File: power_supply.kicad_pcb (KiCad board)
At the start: 2 copper layers, 27 parts, among them T1 Transformer_SP_1S, U1 LM317_TO-220, U2 LM337_TO220, U3 LM385BZ-1.2, U4 LM385BZ-1.2

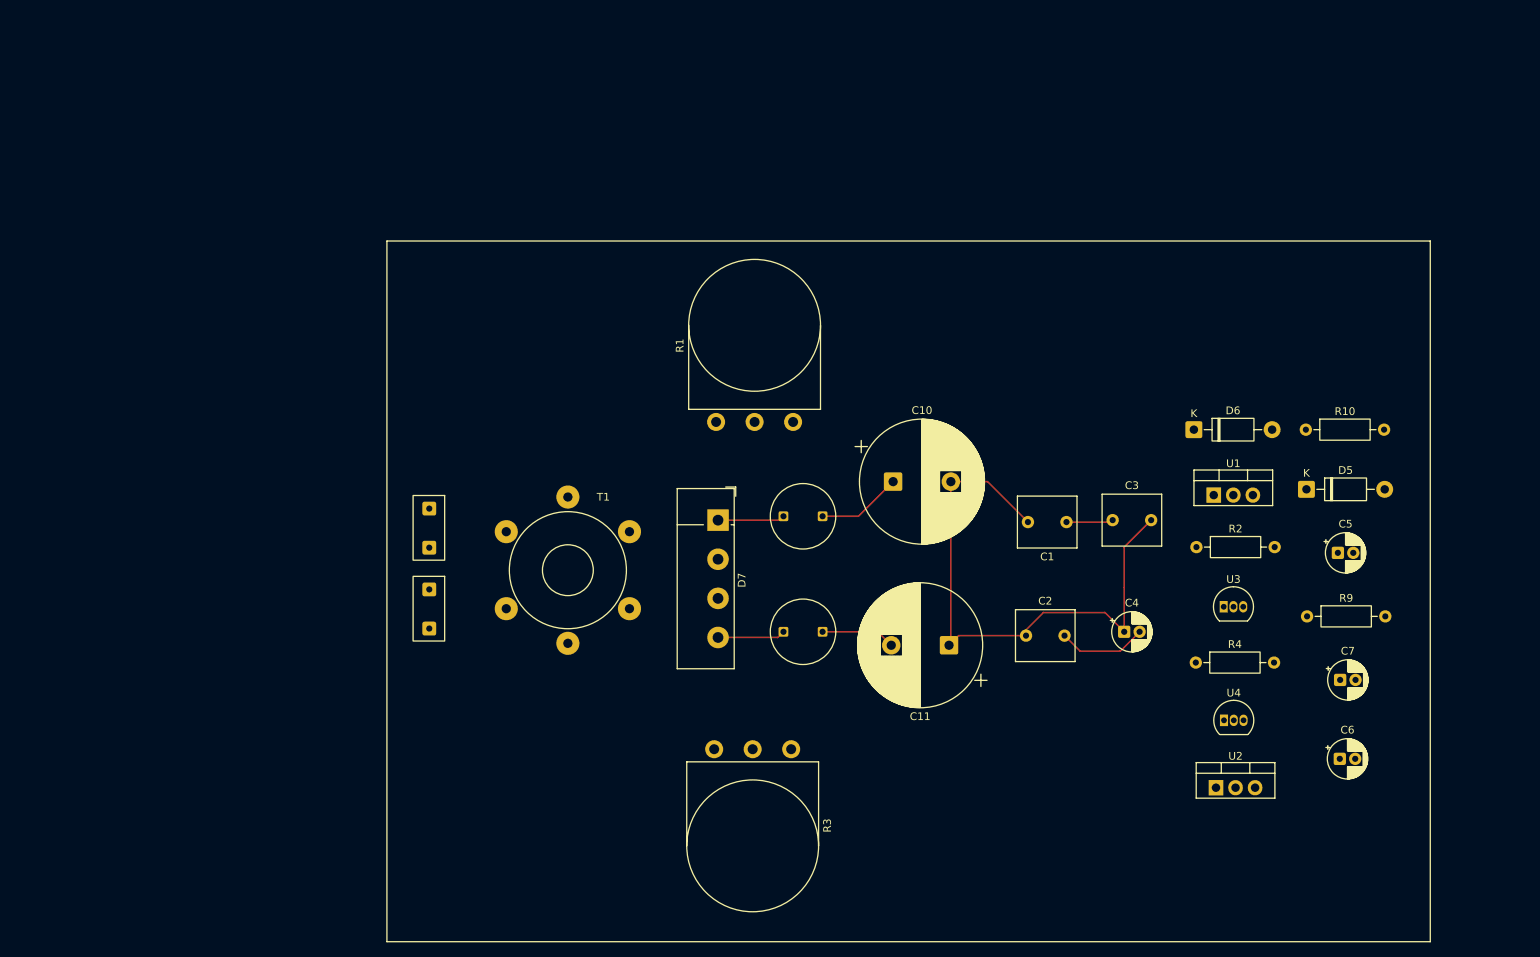
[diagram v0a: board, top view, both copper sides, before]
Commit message: inital version of traces and GND zonefill
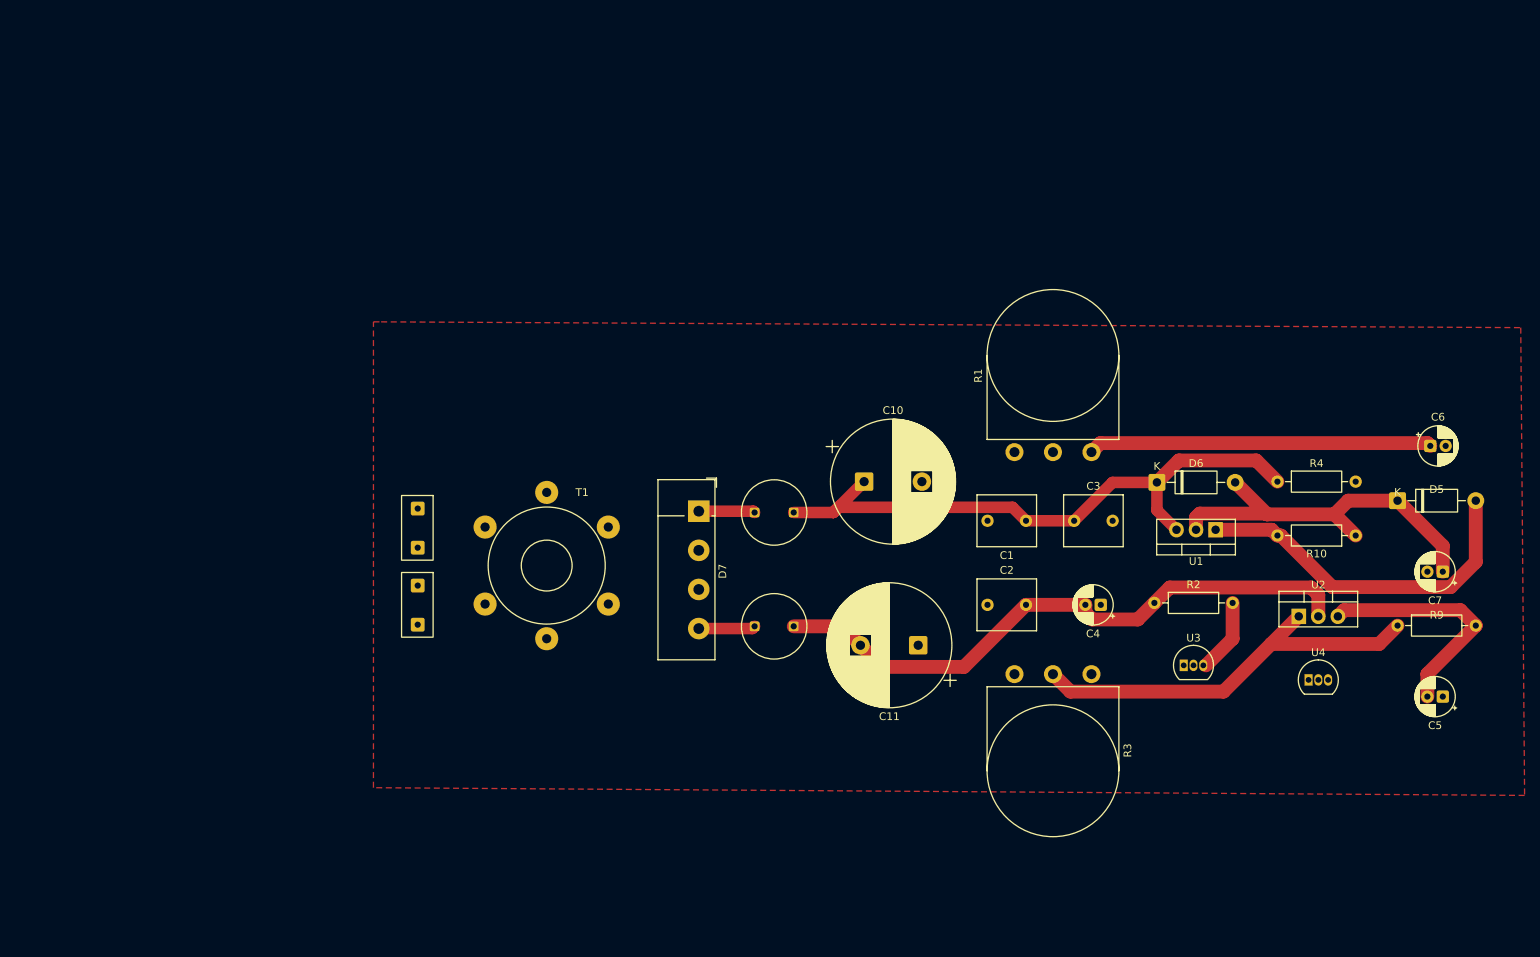
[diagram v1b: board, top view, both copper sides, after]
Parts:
- moved C6 42.3 mm to (211.8, 82.1)
- moved R3 40.2 mm to (157.8, 111.8)
- moved R1 38.9 mm to (167.8, 82.9)
- moved R4 25.8 mm to (191.9, 86.8)
- moved U2 24.7 mm to (194.7, 104.2)
- moved C5 23.1 mm to (213.4, 114.7), turned to 180 degrees
- moved C7 19.4 mm to (213.4, 98.4), turned to 180 degrees
- moved R10 15.2 mm to (202.1, 93.8), turned to 180 degrees
- moved U4 12.2 mm to (195.9, 112.5)
- moved D5 11.9 mm to (207.5, 89.2)
- moved R9 11.8 mm to (207.5, 105.4)
- moved U3 9.21 mm to (179.7, 110.6)
- moved R2 9.08 mm to (175.9, 102.5)
- moved D6 8.36 mm to (176.2, 86.8)
- moved C2 6.40 mm to (154.2, 102.8)
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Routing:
- net Net-(D5-A): track 0.00 -> 90.8 mm
- net GND: track 75.5 -> 0.35 mm
- net Net-(D6-K): track 17.1 -> 82.2 mm
- net Net-(U2-VI): track 21.3 -> 79.9 mm
- net Net-(U2-ADJ): track 0.00 -> 54.3 mm
- net /0-15V: track 0.00 -> 50.2 mm
- net /0-(-15)V: track 0.00 -> 30.9 mm
- net Net-(U3-A): track 0.00 -> 9.63 mm
- net Net-(D7--): track 8.81 -> 7.37 mm
- net Net-(D7-+): track 8.71 -> 7.32 mm
- added copper zone on F.Cu, net GND

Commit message: added connectors, traces and second layer
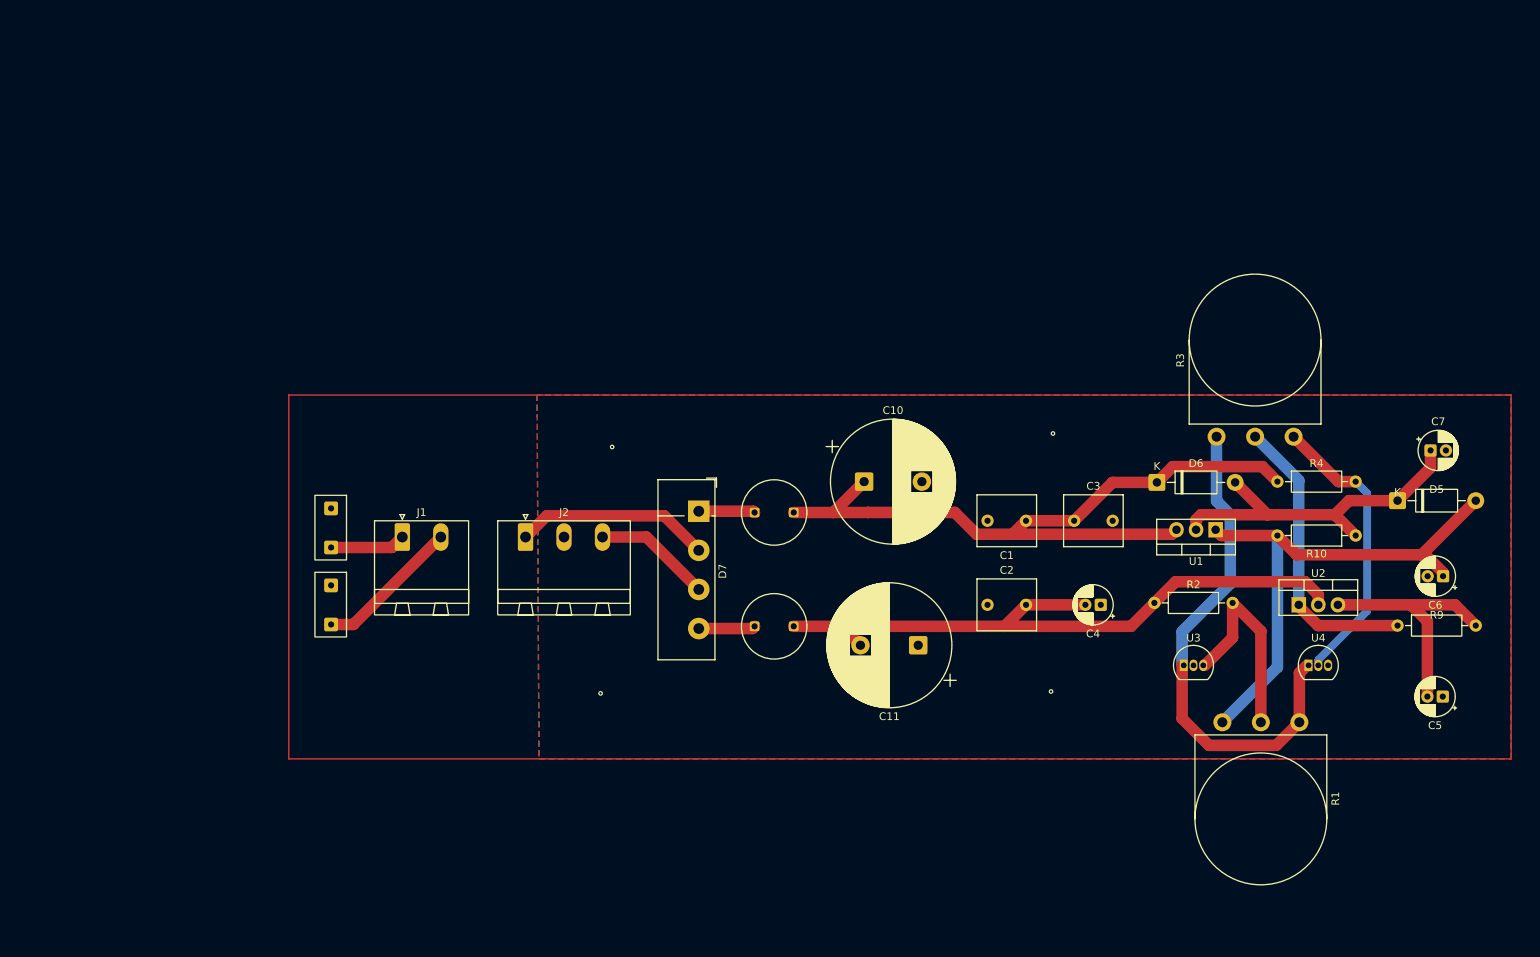
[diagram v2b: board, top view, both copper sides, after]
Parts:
- removed T1: Transformer_SP_1S, Transformer_THT:Transformer_Toroid_Tapped_Horizontal_D14.0mm_Amidon-T50
- added J1: Conn_01x02_Socket, Connector_Phoenix_MSTB:PhoenixContact_MSTBA_2,5_2-G_1x02_P5.00mm_Horizontal, F.Cu at (78.2, 93.9)
- added J2: Conn_01x03_Socket, Connector_Phoenix_MSTB:PhoenixContact_MSTBA_2,5_3-G_1x03_P5.00mm_Horizontal, F.Cu at (94.2, 93.9)
- moved R3 47.6 mm to (194.0, 80.9), turned to 90 degrees
- moved R1 39.0 mm to (184.8, 118.0), turned to -90 degrees
- moved C6 17.0 mm to (213.4, 99.0), turned to 180 degrees
- moved C7 15.8 mm to (211.8, 82.7), turned to 0 degrees
- moved F1 11.3 mm to (69.0, 90.2)
- moved F2 11.3 mm to (69.0, 100.2)
- moved U4 1.89 mm to (195.9, 110.6)
- moved U2 1.50 mm to (194.7, 102.8)
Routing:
- net (no net): track 0.00 -> 65.6 mm
- net Net-(U4-K): track 0.00 -> 37.6 mm
- net Net-(J2-Pin_1): track 0.00 -> 25.5 mm
- net Net-(D5-A): track 90.8 -> 69.5 mm
- net Net-(J1-Pin_2): track 0.00 -> 19.0 mm
- net Net-(U3-A): track 9.63 -> 26.6 mm
- net Net-(U2-ADJ): track 54.3 -> 38.2 mm
- net Net-(J2-Pin_3): track 0.00 -> 15.3 mm
- net Net-(D6-K): track 82.2 -> 95.6 mm
- net Net-(J1-Pin_1): track 0.00 -> 9.81 mm
- net Net-(U2-VI): track 79.9 -> 87.7 mm
- net /0-15V: track 50.2 -> 46.6 mm
- net /0-(-15)V: track 30.9 -> 31.8 mm
- net GND: track 0.35 -> 0.00 mm, vias 0 -> 4
- added copper zone on B.Cu, net GND

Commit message: traces & vias placement corrected
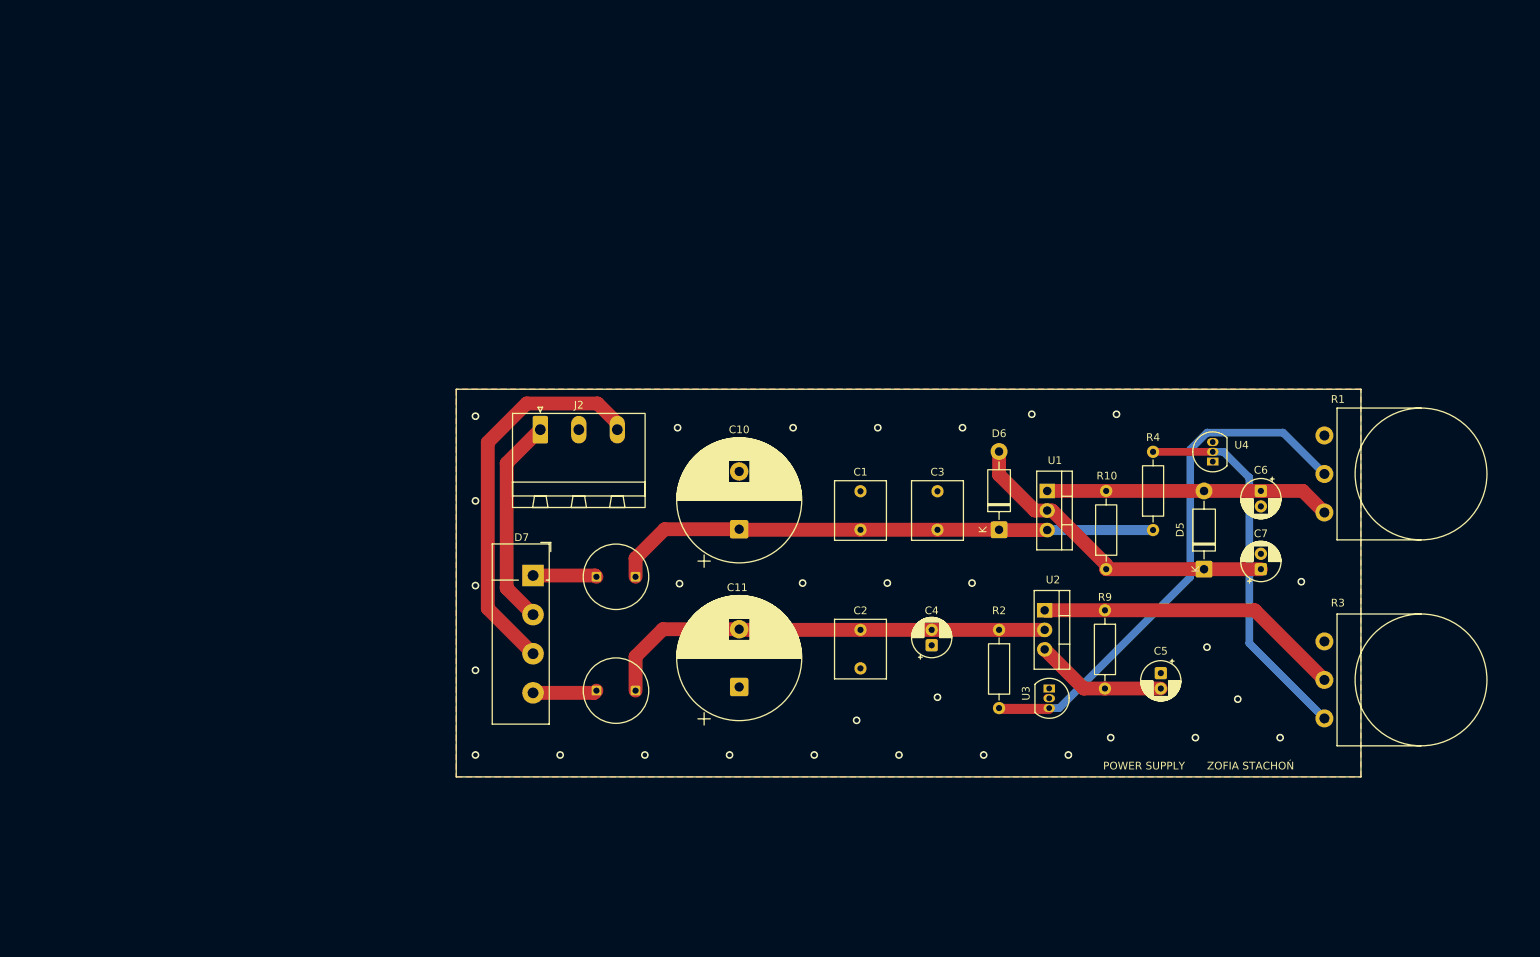
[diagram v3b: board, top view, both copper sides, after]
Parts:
- removed F1, F2: SPT478T, power_supply_own:SPT478T
- removed J1: Conn_01x02_Socket, Connector_Phoenix_MSTB:PhoenixContact_MSTBA_2,5_2-G_1x02_P5.00mm_Horizontal
- moved R9 38.1 mm to (169.5, 103.5), turned to -90 degrees
- moved R3 36.8 mm to (198.0, 117.5), turned to 0 degrees
- moved C5 36.8 mm to (176.8, 111.6), turned to -90 degrees
- moved U2 33.0 mm to (161.7, 103.5), turned to -90 degrees
- moved R10 32.7 mm to (169.7, 98.1), turned to 90 degrees
- moved R1 30.3 mm to (198.0, 90.8), turned to 0 degrees
- moved U4 29.2 mm to (183.5, 84.2), turned to 90 degrees
- moved C7 26.9 mm to (189.8, 98.1), turned to 90 degrees
- moved D5 26.7 mm to (182.4, 98.1), turned to 90 degrees
- moved C6 26.1 mm to (189.8, 88.0), turned to -90 degrees
- moved C11 23.9 mm to (122.0, 113.4), turned to 90 degrees
- moved D7 23.1 mm to (95.2, 98.9)
- moved C4 22.6 mm to (147.0, 108.0), turned to 90 degrees
- moved U1 22.4 mm to (162.0, 88.0), turned to -90 degrees
- moved F3 22.2 mm to (103.5, 99.1)
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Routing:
- net (no net): track 65.6 -> 0.00 mm
- net Net-(U3-A): track 26.6 -> 69.0 mm
- net Net-(J2-Pin_3): track 15.3 -> 50.7 mm
- net Net-(D5-A): track 69.5 -> 37.2 mm
- net Net-(U2-VI): track 87.7 -> 59.1 mm
- net Net-(D6-K): track 95.6 -> 71.2 mm
- net Net-(J1-Pin_2): track 19.0 -> 0.00 mm
- net /0-(-15)V: track 31.8 -> 17.2 mm
- net Net-(U4-K): track 37.6 -> 49.2 mm
- net Net-(J1-Pin_1): track 9.81 -> 0.00 mm
- net /0-15V: track 46.6 -> 42.4 mm
- net Net-(U2-ADJ): track 38.2 -> 40.1 mm
- net Net-(J2-Pin_1): track 25.5 -> 27.3 mm
- net Net-(D7-+): track 7.32 -> 8.30 mm
- net Net-(D7--): track 7.37 -> 8.35 mm
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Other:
- board text added: "POWER SUPPLY"
- board text added: "ZOFIA STACHOŃ"

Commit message: added heatsink footprint
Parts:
- added HS1: Heatsink_Pad_2Pin, power_supply_own:RA-T2X-51E, F.Cu at (36.4, 39.0)
- added HS2: Heatsink_Pad_2Pin, power_supply_own:RA-T2X-51E, F.Cu at (36.4, 65.0)
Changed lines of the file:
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@@
 		)
 	)
+	(footprint "power_supply_own:RA-T2X-51E"
+		(layer "F.Cu")
+		(at 36.35 38.95)
+		(property "Reference" "HS1"
+			(at -5.08 -5.08 0)
+			(unlocked yes)
+			(layer "F.SilkS")
+			(hide yes)
+			(effects
+				(font
+					(size 1 1)
+					(thickness 0.1)
+				)
+			)
+		)
+		(property "Value" "Heatsink_Pad_2Pin"
+			(at 12.7 15.24 0)
+			(unlocked yes)
+			(layer "F.Fab")
+			(effects
+				(font
+					(size 1 1)
+					(thickness 0.15)
+				)
+			)
+		)
+		(property "Datasheet" ""
+			(at 0 0 0)
+			(unlocked yes)
+			(layer "F.Fab")
+			(hide yes)
+			(effects
+				(font
+					(size 1 1)
+					(thickness 0.15)
+				)
+			)
+		)
+		(property "Description" "Heatsink with electrical connection, 2 pin"
+			(at 0 0 0)
+			(unlocked yes)
+			(layer "F.Fab")
+			(hide yes)
+			(effects
+				(font
+					(size 1 1)
+					(thickness 0.15)
+				)
+			)
+		)
+		(property ki_fp_filters "Heatsink_*")
+		(sheetname "/")
+		(sheetfile "power_supply.kicad_sch")
+		(units
+			(unit
+				(name "A")
+				(pins "1" "2")
+			)
+		)
+		(attr smd)
+		(duplicate_pad_numbers_are_jumpers no)
+		(fp_rect
+			(start -8.3 -12.7)
+			(end 33.7 12.3)
+			(stroke
+				(width 0.1)
+				(type default)
+			)
+			(fill no)
+			(layer "F.SilkS")
+		)
+		(pad "1" thru_hole circle
+			(at 0 0)
+			(size 4.5 4.5)
+			(drill 2.6)
+			(layers "*.Cu" "*.Mask")
+			(remove_unused_layers no)
+			(net "GND")
+			(pintype "passive")
+		)
+		(pad "2" thru_hole circle
+			(at 25.4 0)
+			(size 4.5 4.5)
+			(drill 2.6)
+			(layers "*.Cu" "*.Mask")
+			(remove_unused_layers no)
+			(net "GND")
+			(pintype "passive")
+		)
+		(embedded_fonts no)
+	)
 	(footprint "Capacitor_THT:CP_Radial_D16.0mm_P7.50mm"
 		(layer "F.Cu")
@@
 		)
 	)
+	(footprint "power_supply_own:RA-T2X-51E"
+		(layer "F.Cu")
+		(at 36.35 65.05)
+		(property "Reference" "HS2"
+			(at -5.08 -5.08 0)
+			(unlocked yes)
+			(layer "F.SilkS")
+			(hide yes)
+			(effects
+				(font
+					(size 1 1)
+					(thickness 0.1)
+				)
+			)
+		)
+		(property "Value" "Heatsink_Pad_2Pin"
+			(at 12.7 15.24 0)
+			(unlocked yes)
+			(layer "F.Fab")
+			(effects
+				(font
+					(size 1 1)
+					(thickness 0.15)
+				)
+			)
+		)
+		(property "Datasheet" ""
+			(at 0 0 0)
+			(unlocked yes)
+			(layer "F.Fab")
+			(hide yes)
+			(effects
+				(font
+					(size 1 1)
+					(thickness 0.15)
+				)
+			)
+		)
+		(property "Description" "Heatsink with electrical connection, 2 pin"
+			(at 0 0 0)
+			(unlocked yes)
+			(layer "F.Fab")
+			(hide yes)
+			(effects
+				(font
+					(size 1 1)
+					(thickness 0.15)
+				)
+			)
+		)
+		(property ki_fp_filters "Heatsink_*")
+		(sheetname "/")
+		(sheetfile "power_supply.kicad_sch")
+		(units
+			(unit
+				(name "A")
+				(pins "1" "2")
+			)
+		)
+		(attr smd)
+		(duplicate_pad_numbers_are_jumpers no)
+		(fp_rect
+			(start -8.3 -12.7)
+			(end 33.7 12.3)
+			(stroke
+				(width 0.1)
+				(type default)
+			)
+			(fill no)
+			(layer "F.SilkS")
+		)
+		(pad "1" thru_hole circle
+			(at 0 0)
+			(size 4.5 4.5)
+			(drill 2.6)
+			(layers "*.Cu" "*.Mask")
+			(remove_unused_layers no)
+			(net "GND")
+			(pintype "passive")
+		)
+		(pad "2" thru_hole circle
+			(at 25.4 0)
+			(size 4.5 4.5)
+			(drill 2.6)
+			(layers "*.Cu" "*.Mask")
+			(remove_unused_layers no)
+			(net "GND")
+			(pintype "passive")
+		)
+		(embedded_fonts no)
+	)
 	(footprint "Capacitor_THT:CP_Radial_D16.0mm_P7.50mm"
 		(layer "F.Cu")
@@
 	(gr_rect
 		(start 85.25 74.75)
-		(end 202.75 125.095)
+		(end 202.75 129)
 		(stroke
 			(width 0.1)
@@
 		(polygon
 			(pts
-				(xy 85.25 74.75) (xy 85.25 125.095) (xy 202.75 125.095) (xy 202.75 74.75)
+				(xy 85.25 74.75) (xy 85.25 129) (xy 202.75 129) (xy 202.75 74.75)
 			)
 		)
@@
 		(polygon
 			(pts
-				(xy 85.25 74.75) (xy 85.25 125.095) (xy 202.75 125.095) (xy 202.75 74.75)
+				(xy 85.25 74.75) (xy 85.25 129) (xy 202.75 129) (xy 202.75 74.75)
 			)
 		)

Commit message: added circuit with fan
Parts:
- added J1: Conn_01x02_Socket, Connector_Phoenix_MSTB:PhoenixContact_MSTBA_2,5_2-G_1x02_P5.00mm_Horizontal, F.Cu at (79.8, 35.8)
- added J4: Conn_01x03_Socket, Connector_Phoenix_MSTB:PhoenixContact_MSTBA_2,5_3-G_1x03_P5.00mm_Horizontal, F.Cu at (79.8, 50.3)
- added U5: LM7812_TO220, Package_TO_SOT_THT:TO-220-3_Vertical, F.Cu at (97.6, 50.7)

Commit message: pcb final design ver. 1
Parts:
- removed J1: Conn_01x02_Socket, Connector_Phoenix_MSTB:PhoenixContact_MSTBA_2,5_2-G_1x02_P5.00mm_Horizontal
- added J3: Conn_01x02_Socket, Connector_Phoenix_MSTB:PhoenixContact_MSTBA_2,5_2-G_1x02_P5.00mm_Horizontal, F.Cu at (93.1, 95.2)
- moved HS1 128.0 mm to (162.6, 59.8)
- moved J4 106.2 mm to (172.4, 102.2)
- moved HS2 80.8 mm to (117.0, 59.6)
- moved U5 72.4 mm to (154.2, 95.8), turned to 180 degrees
- moved U2 44.5 mm to (127.2, 75.4), turned to 0 degrees
- moved F3 32.1 mm to (98.4, 67.4)
- moved F4 31.7 mm to (98.4, 82.6)
- moved D7 31.6 mm to (92.8, 67.4)
- moved R4 26.8 mm to (149.4, 88.3)
- moved U4 24.0 mm to (160.0, 79.4)
- moved J2 23.0 mm to (100.6, 57.4), turned to 180 degrees
- moved C7 22.0 mm to (168.2, 93.5)
- moved C6 21.8 mm to (168.4, 83.3)
- moved D5 21.3 mm to (161.6, 93.5)
- moved C5 19.4 mm to (161.2, 100.0)
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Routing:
- net /0-(-15)V: track 17.2 -> 92.0 mm
- net Net-(U2-ADJ): track 40.1 -> 101.9 mm
- net Net-(J3-Pin_1): track 0.00 -> 58.2 mm
- net Net-(D6-K): track 71.2 -> 126.0 mm
- net Net-(U4-K): track 49.2 -> 11.9 mm
- net Net-(J2-Pin_3): track 50.7 -> 24.6 mm
- net Net-(D5-A): track 37.2 -> 61.6 mm
- net Net-(U2-VI): track 59.1 -> 83.2 mm
- net /0-15V: track 42.4 -> 64.4 mm
- net Net-(J2-Pin_1): track 27.3 -> 23.4 mm
- net Net-(D7--): track 8.35 -> 5.60 mm
- net Net-(D7-+): track 8.30 -> 5.60 mm
- net Net-(U3-A): track 69.0 -> 71.5 mm
- net GND: track 0.30 -> 0.00 mm, vias 30 -> 0
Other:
- board text removed: "POWER SUPPLY"
- board text removed: "ZOFIA STACHOŃ"
